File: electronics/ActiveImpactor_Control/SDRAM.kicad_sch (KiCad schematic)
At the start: 10 parts, among them U401 W9812G6KH-6

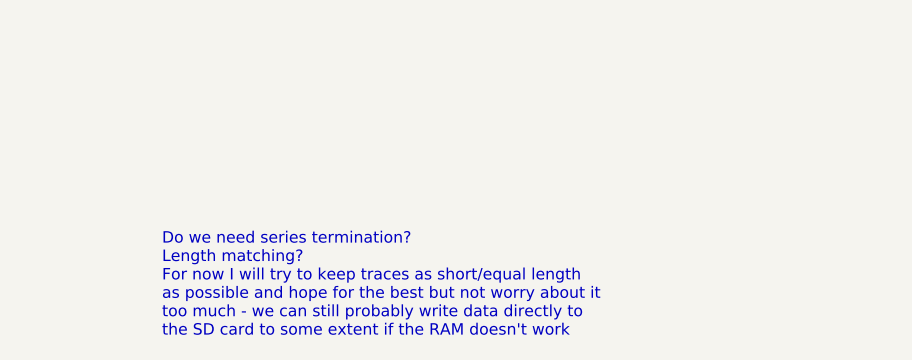
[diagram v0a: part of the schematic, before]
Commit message: added schematics and flexure scripts
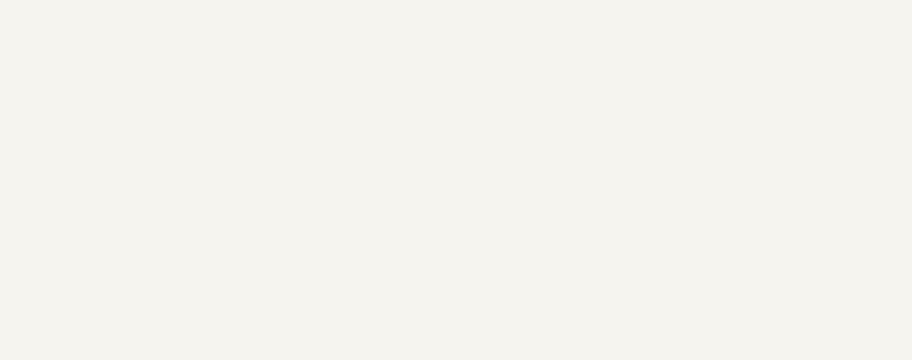
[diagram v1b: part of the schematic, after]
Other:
- note removed: "Do we need series termination? Length matching? For now I will try to keep traces as short/equal length as possible and hope for the best but not worry about it too much - we can still probably write data directly to the SD card to some extent if the RAM doesn't work"
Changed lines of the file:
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@@
-		)
-	)
-	(text "Do we need series termination?\nLength matching?\nFor now I will try to keep traces as short/equal length\nas possible and hope for the best but not worry about it\ntoo much - we can still probably write data directly to \nthe SD card to some extent if the RAM doesn't work"
-		(exclude_from_sim no)
-		(at 115.57 194.31 0)
-		(effects
-			(font
-				(size 1.27 1.27)
-			)
-			(justify left bottom)
 		)
 	)
